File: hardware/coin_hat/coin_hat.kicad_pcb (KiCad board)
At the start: 2 copper layers, 122 x 56.5 mm, 0 parts

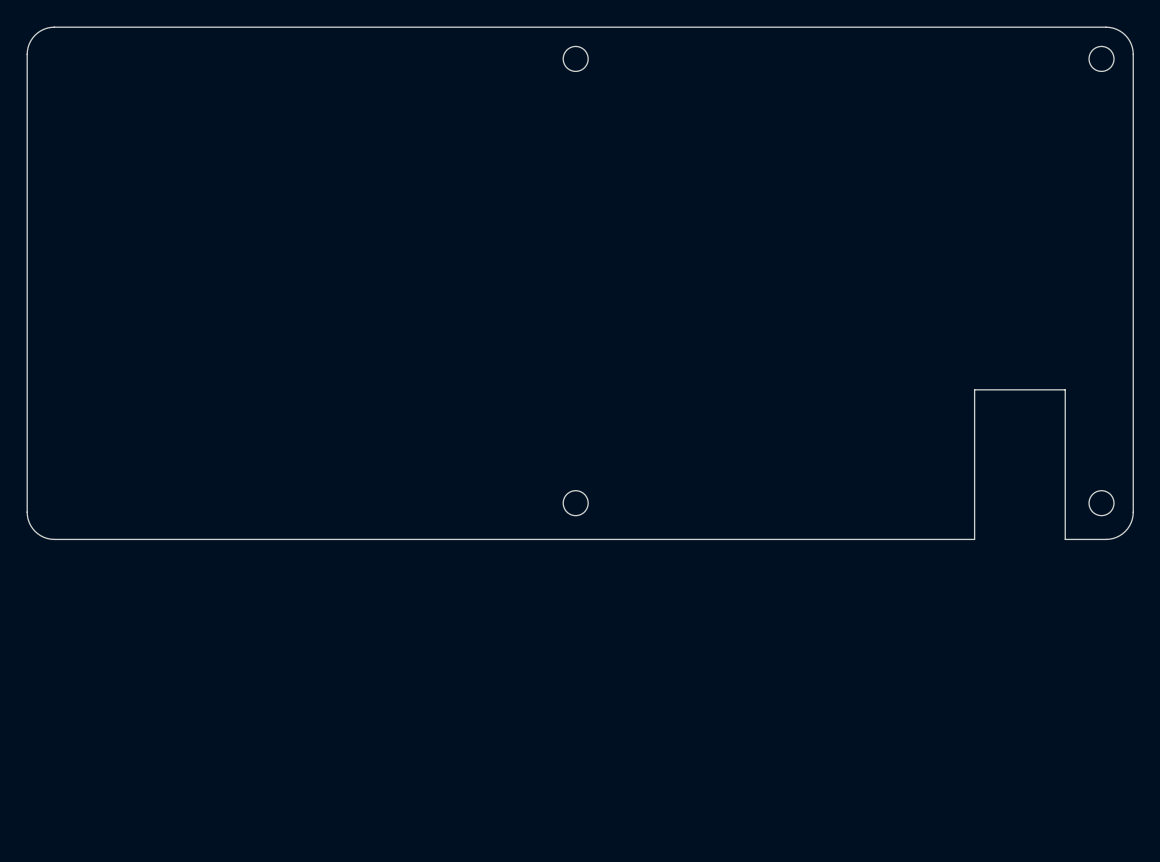
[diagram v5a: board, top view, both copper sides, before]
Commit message: coin_hat: update PCB from schematic and place all footprints
Pull all 56 footprints into the board with their nets and symbol links
(so a GUI Update PCB matches them instead of duplicating), and place
them on the checked floor plan: J1 on the bottom with pin 1 at the
HAT+ position (8.37, 4.77), Pico with USB toward the open +x side,
connectors, fuse and jack on the overhang end.

DRC fixes along the way: move the left-end column up so the jack's
switch pin clears the 0.5 mm edge rule, tighten the two overhang-end
corners to 1 mm so J2/J5 don't overhang the radius, move edge-clipped
reference labels onto their parts, and mark the solder jumpers
not-in-BOM to match their footprints.

DRC: 0 errors, 0 schematic-parity issues, no courtyard overlaps; only
unrouted nets and silkscreen overlaps remain. Ignore *.kicad_prl
(per-user view state).

Co-Authored-By: Claude Opus 5.5 <noreply@anthropic.com>
Claude-Session: https://claude.ai/code/session_01EPngbBgcoS7WRgtdrApT7C
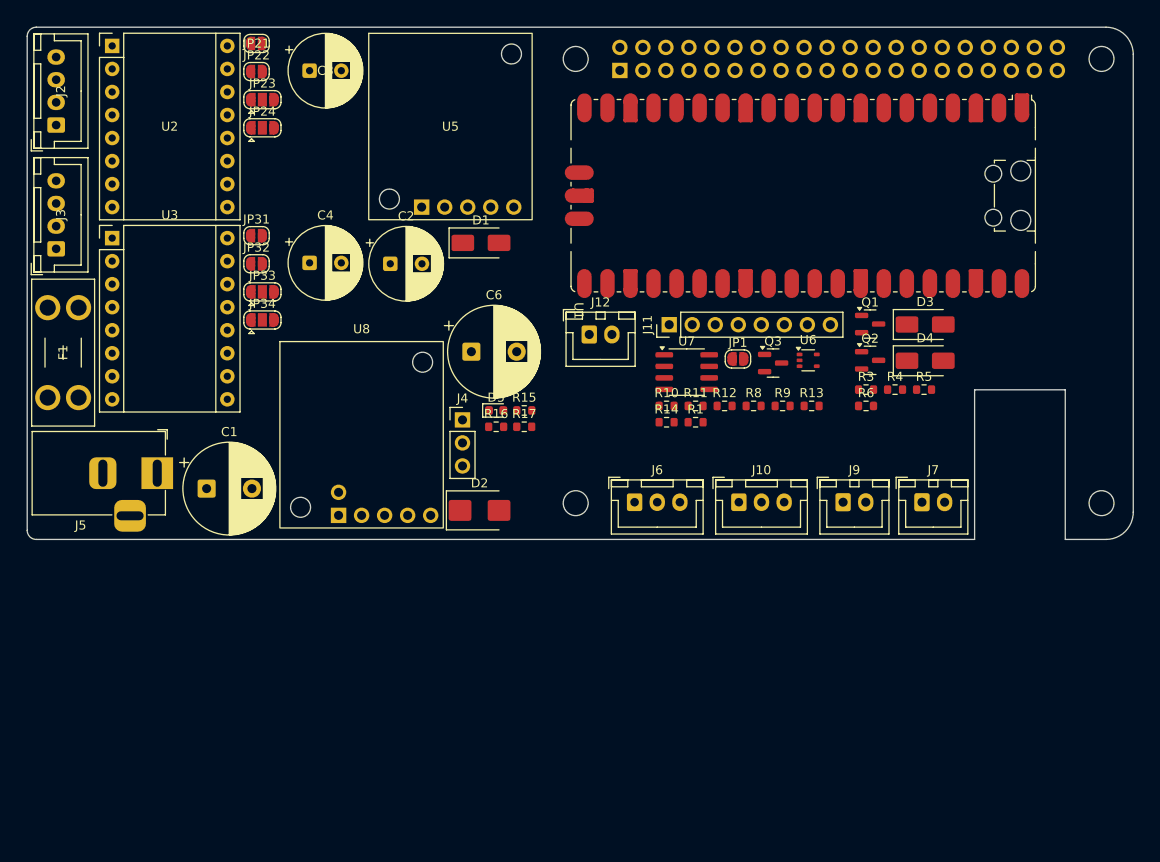
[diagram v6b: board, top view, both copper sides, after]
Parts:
- added C1: 470u/25V, Capacitor_THT:CP_Radial_D10.0mm_P5.00mm, F.Cu at (69.8, 100.9)
- added C2: 100u/10V, Capacitor_THT:CP_Radial_D8.0mm_P3.50mm, F.Cu at (90.0, 76.1)
- added C3: 100u/25V, Capacitor_THT:CP_Radial_D8.0mm_P3.50mm, F.Cu at (81.1, 54.8)
- added C4: 100u/25V, Capacitor_THT:CP_Radial_D8.0mm_P3.50mm, F.Cu at (81.1, 76.0)
- added C6: 1000u/16V (at J4), Capacitor_THT:CP_Radial_D10.0mm_P5.00mm, F.Cu at (99.0, 85.8)
- added D1: SS34, Diode_SMD:D_SMA, F.Cu at (100.0, 73.8)
- added D2: SMBJ15A, Diode_SMD:D_SMB, F.Cu at (99.9, 103.3)
- added D3: SS34, Diode_SMD:D_SMA, F.Cu at (149.0, 82.8)
- added D4: SS34, Diode_SMD:D_SMA, F.Cu at (149.0, 86.8)
- added D5: green (servo rail live), LED_SMD:LED_0603_1608Metric, F.Cu at (101.7, 92.3)
- added F1: 4 A mini blade, Fuse:Fuseholder_Blade_Mini_Keystone_3568, F.Cu at (52.3, 90.9)
- added J1: Pi 40-pin (bottom side), Connector_PinSocket_2.54mm:PinSocket_2x20_P2.54mm_Vertical, B.Cu at (115.4, 54.8)
- added J10: Coin sensor, Connector_JST:JST_XH_B3B-XH-A_1x03_P2.50mm_Vertical, F.Cu at (128.5, 102.4)
- added J11: Aux header, Connector_PinHeader_2.54mm:PinHeader_1x08_P2.54mm_Vertical, F.Cu at (120.8, 82.8)
- added J12: Aux 12V switched, Connector_JST:JST_XH_B2B-XH-A_1x02_P2.50mm_Vertical, F.Cu at (112.0, 83.9)
- added J2: Belt motor, Connector_JST:JST_XH_B4B-XH-A_1x04_P2.50mm_Vertical, F.Cu at (53.2, 60.8)
- added J3: Feeder motor, Connector_JST:JST_XH_B4B-XH-A_1x04_P2.50mm_Vertical, F.Cu at (53.2, 74.4)
- added J4: Diverter servo (1 SIG / 2 V+ / 3 GND), Connector_PinHeader_2.54mm:PinHeader_1x03_P2.54mm_Vertical, F.Cu at (98.0, 93.3)
- added J5: 12 V in 5.5/2.1, Connector_BarrelJack:BarrelJack_Horizontal, F.Cu at (64.3, 99.2)
- added J6: LED ring (WS2812), Connector_JST:JST_XH_B3B-XH-A_1x03_P2.50mm_Vertical, F.Cu at (117.0, 102.4)
- added J7: Key light 12V switched, Connector_JST:JST_XH_B2B-XH-A_1x02_P2.50mm_Vertical, F.Cu at (148.7, 102.4)
- added J9: Home: feeder, Connector_JST:JST_XH_B2B-XH-A_1x02_P2.50mm_Vertical, F.Cu at (140.0, 102.4)
- added JP1: WP->GND to program, Jumper:SolderJumper-2_P1.3mm_Open_RoundedPad1.0x1.5mm, F.Cu at (128.4, 86.6)
- added JP21: MS1 -> 3V3 (closed = high), Jumper:SolderJumper-2_P1.3mm_Open_RoundedPad1.0x1.5mm, F.Cu at (75.3, 51.8)
- added JP22: MS2 -> 3V3 (closed = high), Jumper:SolderJumper-2_P1.3mm_Open_RoundedPad1.0x1.5mm, F.Cu at (75.3, 54.9)
- added JP23: pin4: A=TMC UART / B=3V3 (A4988 MS3), Jumper:SolderJumper-3_P1.3mm_Open_RoundedPad1.0x1.5mm, F.Cu at (75.9, 58.0)
- added JP24: pin6: A=GND (TMC CLK) / B=pin5 (A4988 RST-SLP), Jumper:SolderJumper-3_P1.3mm_Open_RoundedPad1.0x1.5mm, F.Cu at (75.9, 61.1)
- added JP31: MS1 -> 3V3 (closed = high), Jumper:SolderJumper-2_P1.3mm_Open_RoundedPad1.0x1.5mm, F.Cu at (75.3, 73.0)
- added JP32: MS2 -> 3V3 (closed = high), Jumper:SolderJumper-2_P1.3mm_Open_RoundedPad1.0x1.5mm, F.Cu at (75.3, 76.1)
- added JP33: pin4: A=TMC UART / B=3V3 (A4988 MS3), Jumper:SolderJumper-3_P1.3mm_Open_RoundedPad1.0x1.5mm, F.Cu at (75.9, 79.2)
- added JP34: pin6: A=GND (TMC CLK) / B=pin5 (A4988 RST-SLP), Jumper:SolderJumper-3_P1.3mm_Open_RoundedPad1.0x1.5mm, F.Cu at (75.9, 82.3)
- added Q1: AO3400, Package_TO_SOT_SMD:SOT-23, F.Cu at (143.0, 82.7)
- added Q2: AO3400, Package_TO_SOT_SMD:SOT-23, F.Cu at (143.0, 86.7)
- added Q3: AO3400, Package_TO_SOT_SMD:SOT-23, F.Cu at (132.3, 87.0)
- added R1: 1k, Resistor_SMD:R_0603_1608Metric, F.Cu at (123.7, 93.6)
- added R10: 3k9, Resistor_SMD:R_0603_1608Metric, F.Cu at (120.5, 91.8)
- added R11: 3k9, Resistor_SMD:R_0603_1608Metric, F.Cu at (123.7, 91.8)
- added R12: 100k, Resistor_SMD:R_0603_1608Metric, F.Cu at (126.9, 91.8)
- added R13: 100k, Resistor_SMD:R_0603_1608Metric, F.Cu at (136.5, 91.8)
- added R14: 15k, Resistor_SMD:R_0603_1608Metric, F.Cu at (120.5, 93.6)
- added R15: 1k, Resistor_SMD:R_0603_1608Metric, F.Cu at (104.8, 92.3)
- added R16: 10k, Resistor_SMD:R_0603_1608Metric, F.Cu at (101.7, 94.1)
- added R17: 10k, Resistor_SMD:R_0603_1608Metric, F.Cu at (104.8, 94.1)
- added R3: 100R, Resistor_SMD:R_0603_1608Metric, F.Cu at (142.5, 90.0)
- added R4: 10k, Resistor_SMD:R_0603_1608Metric, F.Cu at (145.7, 90.0)
- added R5: 100R, Resistor_SMD:R_0603_1608Metric, F.Cu at (148.9, 90.0)
- added R6: 10k, Resistor_SMD:R_0603_1608Metric, F.Cu at (142.5, 91.8)
- added R8: 1k, Resistor_SMD:R_0603_1608Metric, F.Cu at (130.1, 91.8)
- added R9: 10k, Resistor_SMD:R_0603_1608Metric, F.Cu at (133.3, 91.8)
- added U1: Raspberry Pi Pico, Module:RaspberryPi_Pico_SMD_HandSolder, F.Cu at (135.6, 68.6)
- added U2: StepStick (TMC2209 or A4988), Module:Pololu_Breakout-16_15.2x20.3mm, F.Cu at (59.4, 52.1)
- added U3: StepStick (TMC2209 or A4988), Module:Pololu_Breakout-16_15.2x20.3mm, F.Cu at (59.4, 73.3)
- added U5: Pololu D24V50F5 (12V->5V 5A), coin_hat:Pololu_D24V50F5, F.Cu at (93.5, 69.8)
- added U6: 74AHCT1G125, Package_TO_SOT_SMD:SOT-353_SC-70-5, F.Cu at (136.1, 86.7)
- added U7: CAT24C32, Package_SO:SOIC-8_3.9x4.9mm_P1.27mm, F.Cu at (122.7, 88.0)
- added U8: Pololu D36V28F6 (12V->6V servo) or F5, coin_hat:Pololu_D36V28Fx, F.Cu at (84.3, 103.8)
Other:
- outline, holes or cut-outs redrawn
- board text added: "Footprints placed on the checked floor plan (courtyards clear). 16 mm spacers. Pi + HAT stack 142 x 56.5."
- board text removed: "C1"
- board text removed: "C2"
- board text removed: "C3"
- board text removed: "C4"
- board text removed: "C6"
- board text removed: "D1"
- board text removed: "D2"
- board text removed: "D5 R15-17"
- board text removed: "F1"
- board text removed: "Floor plan = real courtyards (incl. coin_hat:Pololu_* footprints), checked for overlaps. 16 mm spacers. Pi + HAT stack 142 x 56.5."
- board text removed: "J10"
- board text removed: "J11"
- board text removed: "J12"
- board text removed: "J2"
- board text removed: "J3"
- board text removed: "J4"
- board text removed: "J5 jack (plug from left)"
- board text removed: "J6"
- board text removed: "J7"
- board text removed: "J9"
- board text removed: "JP21-24"
- board text removed: "JP31-34"
- board text removed: "Q1 Q2 D3 D4"
- board text removed: "Q3 U6 U7 JP1 R1-R14"
- board text removed: "U1 Pico"
- board text removed: "U2"
- board text removed: "U3"
- board text removed: "U5 5V buck D24V50F5"
- board text removed: "U8 servo buck D36V28Fx"

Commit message: coin_hat: route the board and generate JLCPCB / PCBWay files
Fully routed 2-layer board, KiCad 9 DRC clean (0 violations, 0
unconnected, 0 schematic-parity issues). Freerouting did the bulk; the
Pi 5V feed to J1 pins 2/4 is hand-placed and locked (1.5 mm, necking to
1.0 mm past the mounting hole). Net classes for high-current, power,
motor and ground nets, GND poured on both layers, and copper keepouts
under the HAT+ standoffs (3.1 mm bottom, 2.6 mm top).

Placement changes to make it route: driver column 1 mm right, Pico and
its neighbours 1.5 mm down, gate resistors spread out. J5 becomes the
CUI PJ-102AH footprint (same pad pattern, 5 A rated).

Schematic symbols now carry LCSC / Manufacturer / MPN fields (JLCPCB
basic parts where available). make_fab.py writes fab/: a Gerber + drill
zip, JLCPCB BOM + CPL (SMD only, rotation corrections applied) and a
PCBWay BOM + centroid.

Co-Authored-By: Claude Opus 5.5 <noreply@anthropic.com>
Claude-Session: https://claude.ai/code/session_01EPngbBgcoS7WRgtdrApT7C
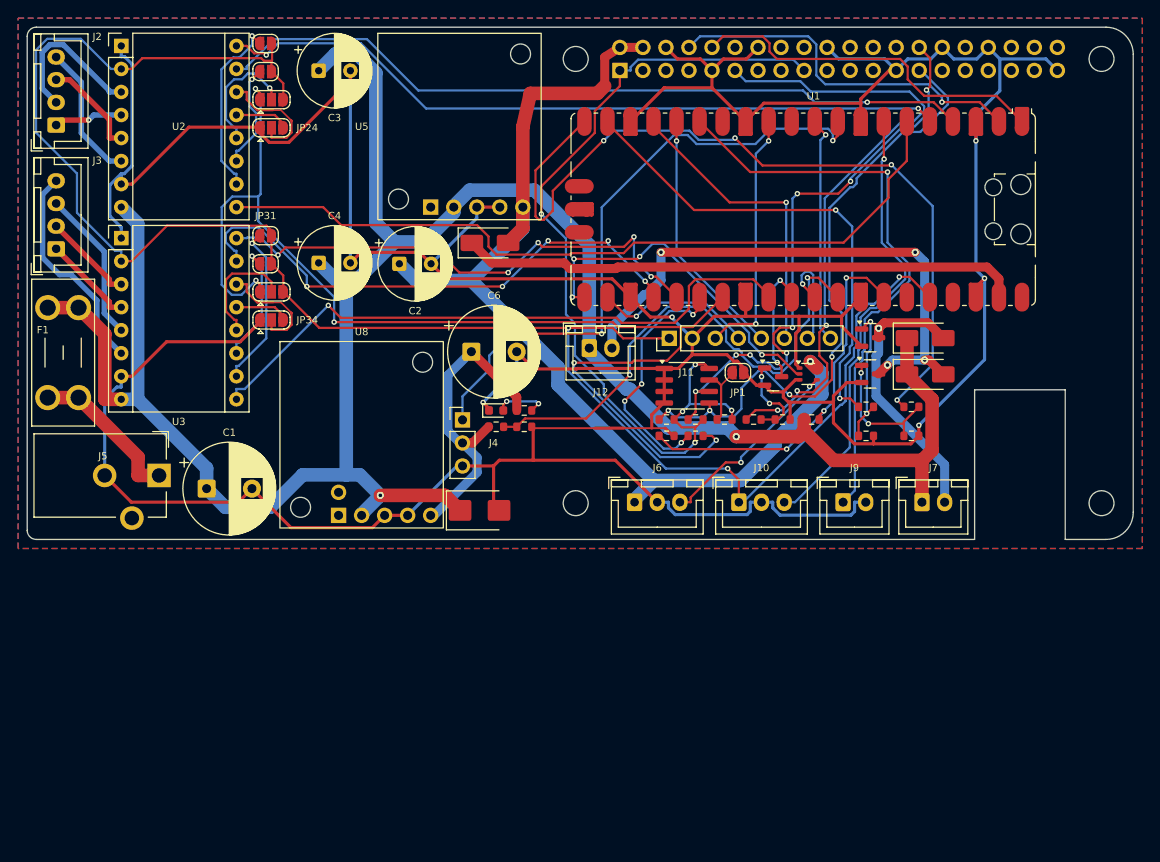
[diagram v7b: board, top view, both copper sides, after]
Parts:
- J5: value 12 V in 5.5/2.1 -> 12 V in 5.5/2.1 (CUI PJ-102AH, 5 A); footprint Connector_BarrelJack:BarrelJack_Horizontal -> Connector_BarrelJack:BarrelJack_CUI_PJ-102AH_Horizontal
- U7: value CAT24C32 -> M24C32-RMN6TP
- moved R4 6.02 mm to (142.5, 95.1)
- moved R6 5.99 mm to (147.5, 95.1)
- moved R5 2.36 mm to (147.5, 91.9)
- moved R3 1.90 mm to (142.5, 91.9)
- moved D3 1.50 mm to (149.0, 84.3)
- moved D4 1.50 mm to (149.0, 88.3)
- moved J11 1.50 mm to (120.8, 84.3)
- moved J12 1.50 mm to (112.0, 85.4)
- moved JP1 1.50 mm to (128.4, 88.1)
- moved Q1 1.50 mm to (143.0, 84.2)
- moved Q2 1.50 mm to (143.0, 88.2)
- moved Q3 1.50 mm to (132.3, 88.5)
- moved R1 1.50 mm to (123.7, 95.1)
- moved R10 1.50 mm to (120.5, 93.3)
- moved R11 1.50 mm to (123.7, 93.3)
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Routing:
- net GND: track 0.00 -> 526.8 mm, vias 0 -> 5
- net +12V: track 0.00 -> 249.6 mm, vias 0 -> 2
- net +3V3: track 0.00 -> 201.5 mm, vias 0 -> 3
- net TMC_UART: track 0.00 -> 132.5 mm, vias 0 -> 5
- net +5V: track 0.00 -> 114.2 mm, vias 0 -> 1
- net PI_3V3: track 0.00 -> 97.2 mm, vias 0 -> 5
- net AUX_PWM: track 0.00 -> 89.8 mm, vias 0 -> 4
- net BELT_EN: track 0.00 -> 86.6 mm
- net BELT_STEP: track 0.00 -> 84.3 mm, vias 0 -> 1
- net BELT_DIR: track 0.00 -> 81.1 mm, vias 0 -> 2
- net ID_SD: track 0.00 -> 69.8 mm, vias 0 -> 4
- net PI_RESET_PICO: track 0.00 -> 69.8 mm, vias 0 -> 3
- net SERVO_PWM: track 0.00 -> 68.9 mm, vias 0 -> 3
- net FEED_EN: track 0.00 -> 68.9 mm, vias 0 -> 1
- net ID_SC: track 0.00 -> 65.2 mm, vias 0 -> 8
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- added copper zone on B.Cu, net GND
- added copper zone on F.Cu, net GND

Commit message: coin_hat: pre-fab review fixes
- Move the Pico so its micro-USB socket is at the board edge; 9 mm of
  board sat in the footprint's USB-cable keepout and would have blocked
  the plug used for REPL / mpremote.
- Add 100 nF bypass caps C7 (U6 level shifter) and C8 (U7 HAT+ EEPROM),
  JLCPCB basic part C14663.
- Power-net vias 1.2/0.6 mm (~3 A); the switched outputs and the TVS
  each went through a single 0.4 mm via. One AUX_SW via stays 0.8/0.4
  for clearance, so J12 is rated ~1.5 A.
- Remove paste from the Pico pads (not fab-assembled).
- Move the EEPROM group into the pocket left of the Pico; the board now
  routes completely.

KiCad 9: ERC 0 errors, DRC 0 errors / 0 unconnected / 0 parity issues
(the Pico "differs from library" warning is the paste change). fab/
regenerated. README notes the J1 socket height needed for 16 mm
spacers, 12 V-only powering, and the jumper label order.

Co-Authored-By: Claude Opus 5.5 <noreply@anthropic.com>
Claude-Session: https://claude.ai/code/session_01EPngbBgcoS7WRgtdrApT7C
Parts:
- added C7: 100n (U6 bypass), Capacitor_SMD:C_0603_1608Metric, F.Cu at (138.7, 88.3)
- added C8: 100n (U7 bypass), Capacitor_SMD:C_0603_1608Metric, F.Cu at (116.7, 63.5)
- moved U7 25.8 mm to (112.7, 65.7), turned to 90 degrees
- moved R12 24.5 mm to (114.8, 72.0), turned to 90 degrees
- moved R11 23.9 mm to (112.8, 72.0), turned to 90 degrees
- moved R10 23.4 mm to (110.8, 72.0), turned to 90 degrees
- moved JP1 20.7 mm to (111.7, 75.8)
- moved U1 9.00 mm to (144.6, 70.1)
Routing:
- net GND: track 526.8 -> 577.9 mm, vias 5 -> 15
- net PI_3V3: track 97.2 -> 51.4 mm, vias 5 -> 2
- net AUX_PWM: track 89.8 -> 58.5 mm
- net PI_RESET_PICO: track 69.8 -> 45.4 mm
- net SERVO_PWM: track 68.9 -> 92.7 mm
- net SERVO_SENSE: track 58.1 -> 81.2 mm
- net TMC_UART: track 132.5 -> 110.7 mm, vias 5 -> 6
- net VSYS_PICO: track 61.9 -> 79.9 mm
- net BELT_DIR: track 81.1 -> 96.0 mm, vias 2 -> 1
- net RING_DATA: track 38.0 -> 23.2 mm, vias 4 -> 0
- net BELT_STEP: track 84.3 -> 97.5 mm, vias 1 -> 3
- net AUX_SW: track 61.7 -> 74.0 mm, vias 4 -> 2
- net EEPROM_WP: track 7.49 -> 19.5 mm, vias 0 -> 2
- net PI_TXD: track 40.9 -> 52.8 mm
- net ID_SD: track 69.8 -> 58.4 mm, vias 4 -> 2
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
